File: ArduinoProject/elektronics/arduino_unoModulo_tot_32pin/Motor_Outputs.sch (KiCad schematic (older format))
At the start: 9 parts, among them J501 Conn_01x04_Female

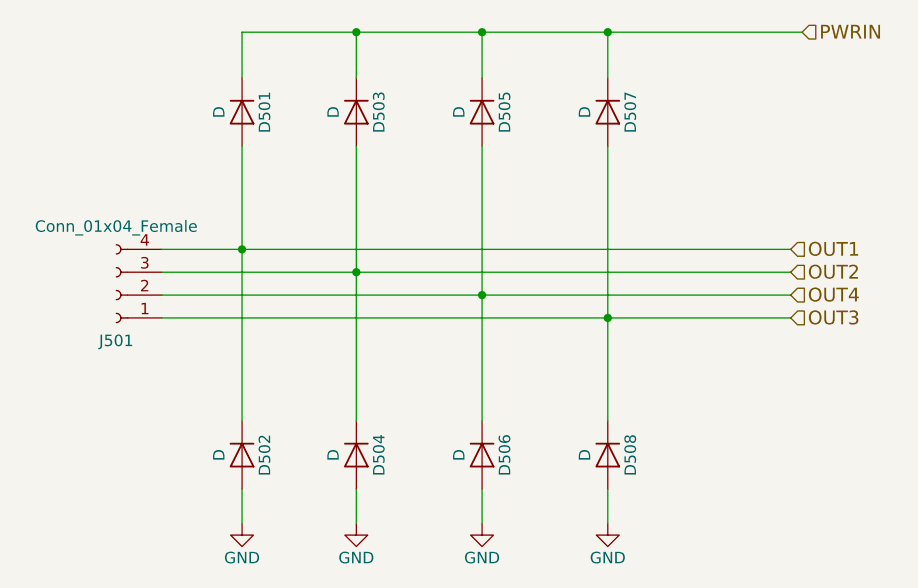
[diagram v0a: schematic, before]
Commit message: sensormodule_x4 added
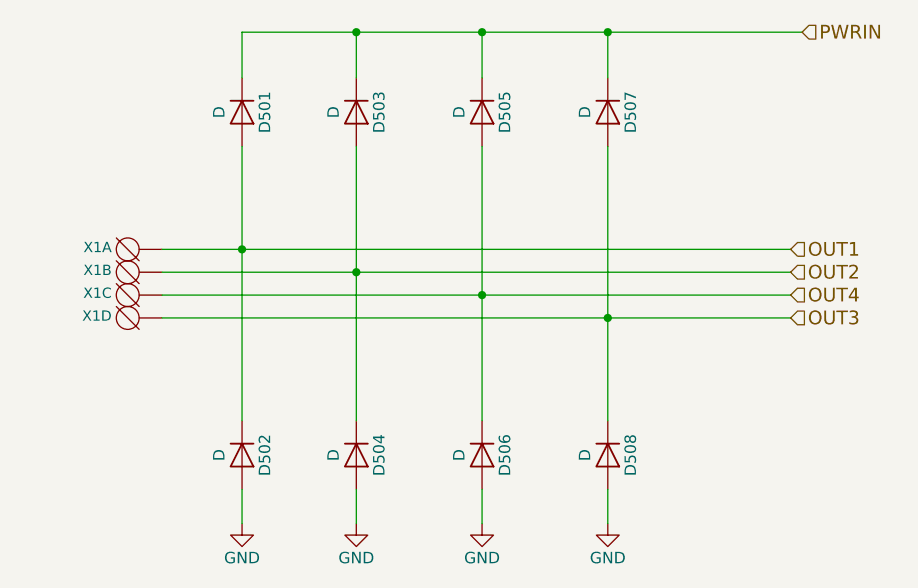
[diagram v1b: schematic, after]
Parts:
- removed J501: Conn_01x04_Female, Socket_Strips:Socket_Strip_Angled_1x04_Pitch2.00mm, symbol Conn_01x04_Female
- added X1: DG3XX-04-3.5, degson_DG350-3.5-04P, symbol DG3XX-04-3.5
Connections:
- net OUT1: now also X1.1 (KL)
- net OUT2: now also X1.2 (KL)
- net OUT3: now also X1.4 (KL)
- net OUT4: now also X1.3 (KL)
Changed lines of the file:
@@
 LIBS:MFN_Atmel
 LIBS:MFN_STMicro
+LIBS:degson
 LIBS:Arduino_Uno_R3_From_Scratch-cache
 EELAYER 25 0
@@
 	0    1    1    0
 $EndComp
-$Comp
-L Conn_01x04_Female J501
-U 1 1 5A968F72
-P 3650 3600
-F 0 "J501" H 3650 3800 50  0000 C CNN
-F 1 "Conn_01x04_Female" H 3650 3300 50  0000 C CNN
-F 2 "Socket_Strips:Socket_Strip_Angled_1x04_Pitch2.00mm" H 3650 3600 50  0001 C CNN
-F 3 "" H 3650 3600 50  0001 C CNN
-	1    3650 3600
-	-1   0    0    1
-$EndComp
 Wire Wire Line
 	3850 3400 6600 3400
@@
 Wire Wire Line
 	5800 4600 5800 4450
-Wire Wire Line
-	5250 4450 5250 4600
 Wire Wire Line
 	4700 4600 4700 4450
@@
 Text HLabel 6650 2450 2    60   Input ~ 0
 PWRIN
+Wire Wire Line
+	5250 4600 5250 4450
+$Comp
+L DG3XX-04-3.5 X1
+U 1 1 5AA04257
+P 3750 3400
+F 0 "X1" H 3870 3365 45  0000 L BNN
+F 1 "DG3XX-04-3.5" H 3750 3400 45  0001 L BNN
+F 2 "degson_DG350-3.5-04P" H 3780 3550 20  0001 C CNN
+F 3 "" H 3750 3400 60  0001 C CNN
+	1    3750 3400
+	-1   0    0    1
+$EndComp
+$Comp
+L DG3XX-04-3.5 X1
+U 2 1 5AA042B2
+P 3750 3500
+F 0 "X1" H 3870 3465 45  0000 L BNN
+F 1 "DG3XX-04-3.5" H 3750 3500 45  0001 L BNN
+F 2 "degson_DG350-3.5-04P" H 3780 3650 20  0001 C CNN
+F 3 "" H 3750 3500 60  0001 C CNN
+	2    3750 3500
+	-1   0    0    1
+$EndComp
+$Comp
+L DG3XX-04-3.5 X1
+U 3 1 5AA04319
+P 3750 3600
+F 0 "X1" H 3870 3565 45  0000 L BNN
+F 1 "DG3XX-04-3.5" H 3750 3600 45  0001 L BNN
+F 2 "degson_DG350-3.5-04P" H 3780 3750 20  0001 C CNN
+F 3 "" H 3750 3600 60  0001 C CNN
+	3    3750 3600
+	-1   0    0    1
+$EndComp
+$Comp
+L DG3XX-04-3.5 X1
+U 4 1 5AA043AC
+P 3750 3700
+F 0 "X1" H 3870 3665 45  0000 L BNN
+F 1 "DG3XX-04-3.5" H 3750 3700 45  0001 L BNN
+F 2 "degson_DG350-3.5-04P" H 3780 3850 20  0001 C CNN
+F 3 "" H 3750 3700 60  0001 C CNN
+	4    3750 3700
+	-1   0    0    1
+$EndComp
 $EndSCHEMATC

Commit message: arduino routed
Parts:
- X1: footprint degson_DG350-3.5-04P -> degson:degson-DG350-3.5-04P
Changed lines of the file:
@@
 F 0 "X1" H 3870 3365 45  0000 L BNN
 F 1 "DG3XX-04-3.5" H 3750 3400 45  0001 L BNN
-F 2 "degson_DG350-3.5-04P" H 3780 3550 20  0001 C CNN
+F 2 "degson:degson-DG350-3.5-04P" H 3780 3550 20  0001 C CNN
 F 3 "" H 3750 3400 60  0001 C CNN
 	1    3750 3400
@@
 F 0 "X1" H 3870 3465 45  0000 L BNN
 F 1 "DG3XX-04-3.5" H 3750 3500 45  0001 L BNN
-F 2 "degson_DG350-3.5-04P" H 3780 3650 20  0001 C CNN
+F 2 "degson:degson-DG350-3.5-04P" H 3780 3650 20  0001 C CNN
 F 3 "" H 3750 3500 60  0001 C CNN
 	2    3750 3500
@@
 F 0 "X1" H 3870 3565 45  0000 L BNN
 F 1 "DG3XX-04-3.5" H 3750 3600 45  0001 L BNN
-F 2 "degson_DG350-3.5-04P" H 3780 3750 20  0001 C CNN
+F 2 "degson:degson-DG350-3.5-04P" H 3780 3750 20  0001 C CNN
 F 3 "" H 3750 3600 60  0001 C CNN
 	3    3750 3600
@@
 F 0 "X1" H 3870 3665 45  0000 L BNN
 F 1 "DG3XX-04-3.5" H 3750 3700 45  0001 L BNN
-F 2 "degson_DG350-3.5-04P" H 3780 3850 20  0001 C CNN
+F 2 "degson:degson-DG350-3.5-04P" H 3780 3850 20  0001 C CNN
 F 3 "" H 3750 3700 60  0001 C CNN
 	4    3750 3700
